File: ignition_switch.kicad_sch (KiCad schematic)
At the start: 8 parts, among them U11 EL3H7, U9 EL3H7

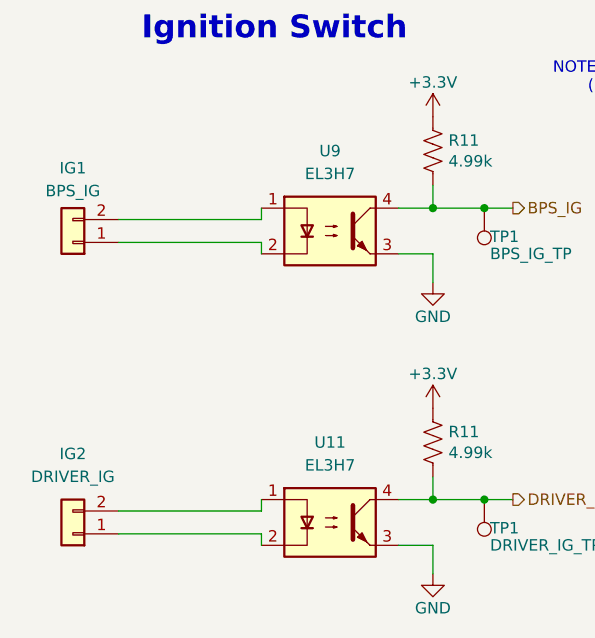
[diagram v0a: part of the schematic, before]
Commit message: Changed optocoupler resistor values, updated Mouser PNs
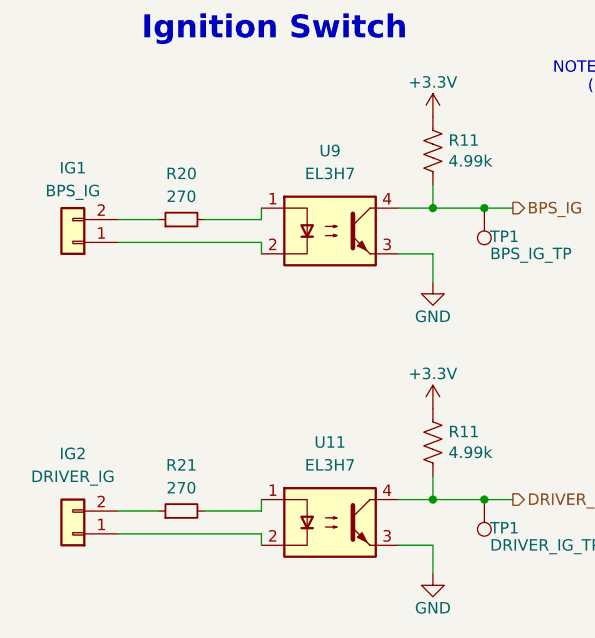
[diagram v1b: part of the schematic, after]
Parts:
- added R20, R21: 270, Resistor_SMD:R_0805_2012Metric, symbol Device:R_Small
- IG1, IG2: Mouser PN (none) -> 538-43650-0215
- R11: Mauser PN 71-CRCW08054K99FKEAC -> (none); Mouser PN (none) -> 71-CRCW08054K99FKEAC
- U11, U9: Mauser PN 638-EL3H7DTAVG -> (none); Mouser PN (none) -> 638-EL3H7DTAVG
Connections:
- net at IG1.2 (Pin_2): now also R20.1; no longer U9.1
- net at U11.1: now also R21.2; no longer IG2.2 (Pin_2)
- new net: IG2.2 (Pin_2), R21.1
- new net: R20.2, U9.1
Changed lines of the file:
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@@
+    (stroke (width 0) (type default))
+  )
+  (wire (pts (xy 122.555 106.68) (xy 128.905 106.68))
     (stroke (width 0) (type default))
   )
@@
     (stroke (width 0) (type default))
   )
-  (wire (pts (xy 113.03 74.295) (xy 128.905 74.295))
+  (wire (pts (xy 122.555 74.295) (xy 128.905 74.295))
+    (stroke (width 0) (type default))
+  )
+  (wire (pts (xy 113.03 74.295) (xy 117.475 74.295))
     (stroke (width 0) (type default))
   )
@@
     (stroke (width 0) (type default))
   )
-  (wire (pts (xy 113.03 106.68) (xy 128.905 106.68))
+  (wire (pts (xy 113.03 106.68) (xy 117.475 106.68))
     (stroke (width 0) (type default))
   )
@@
       (effects (font (size 1.27 1.27)) hide)
     )
+    (property "Mouser PN" "538-43650-0215" (at 107.95 76.835 0)
+      (effects (font (size 1.27 1.27)) hide)
+    )
     (pin "1")
     (pin "2")
@@
       (effects (font (size 1.27 1.27)) (justify left) hide)
     )
-    (property "Mauser PN" "638-EL3H7DTAVG " (at 136.525 107.95 0)
-      (effects (font (size 1.27 1.27)) hide)
-    )
     (property "PN" "EL3H7(D)(TA)-VG" (at 136.525 107.95 0)
+      (effects (font (size 1.27 1.27)) hide)
+    )
+    (property "Mouser PN" "638-EL3H7DTAVG " (at 136.525 107.95 0)
       (effects (font (size 1.27 1.27)) hide)
     )
@@
     )
   )
+  (symbol (lib_id "Device:R_Small") (at 120.015 106.68 90) (unit 1)
+    (in_bom yes) (on_board yes) (dnp no) (fields_autoplaced)
+    (property "Reference" "R21" (at 120.015 101.6 90)
+      (effects (font (size 1.27 1.27)))
+    )
+    (property "Value" "270" (at 120.015 104.14 90)
+      (effects (font (size 1.27 1.27)))
+    )
+    (property "Footprint" "Resistor_SMD:R_0805_2012Metric" (at 120.015 106.68 0)
+      (effects (font (size 1.27 1.27)) hide)
+    )
+    (property "Datasheet" "https://www.vishay.com/docs/20065/rcse3.pdf" (at 120.015 106.68 0)
+      (effects (font (size 1.27 1.27)) hide)
+    )
+    (property "Mouser PN" "71-RCS0805270RFKEA" (at 120.015 106.68 90)
+      (effects (font (size 1.27 1.27)) hide)
+    )
+    (property "PN" "RCS0805270RFKEA" (at 120.015 106.68 90)
+      (effects (font (size 1.27 1.27)) hide)
+    )
+    (pin "1")
+    (pin "2")
+    (instances
+      (project "Controls-LeaderDaughterPCB"
+        (path "/c7871779-04fe-4705-8150-20a4dd0ef44f/0d7b9330-5178-458e-b803-9c8d464fd559"
+          (reference "R21") (unit 1)
+        )
+      )
+    )
+  )
   (symbol (lib_id "Isolator:EL817") (at 136.525 75.565 0) (unit 1)
     (in_bom yes) (on_board yes) (dnp no) (fields_autoplaced)
@@
       (effects (font (size 1.27 1.27)) (justify left) hide)
     )
-    (property "Mauser PN" "638-EL3H7DTAVG " (at 136.525 75.565 0)
-      (effects (font (size 1.27 1.27)) hide)
-    )
     (property "PN" "EL3H7(D)(TA)-VG" (at 136.525 75.565 0)
+      (effects (font (size 1.27 1.27)) hide)
+    )
+    (property "Mouser PN" "638-EL3H7DTAVG " (at 136.525 75.565 0)
       (effects (font (size 1.27 1.27)) hide)
     )
@@
       (effects (font (size 1.27 1.27)) hide)
     )
+    (property "Mouser PN" "538-43650-0215" (at 107.95 109.22 0)
+      (effects (font (size 1.27 1.27)) hide)
+    )
     (pin "1")
     (pin "2")
@@
       (effects (font (size 1.27 1.27)) hide)
     )
-    (property "Mauser PN" "71-CRCW08054K99FKEAC " (at 147.955 66.675 0)
+    (property "Mouser PN" "71-CRCW08054K99FKEAC " (at 147.955 66.675 0)
       (effects (font (size 1.27 1.27)) hide)
     )
@@
       (effects (font (size 1.27 1.27)) hide)
     )
-    (property "Mauser PN" "71-CRCW08054K99FKEAC " (at 147.955 99.06 0)
+    (property "Mouser PN" "71-CRCW08054K99FKEAC " (at 147.955 99.06 0)
       (effects (font (size 1.27 1.27)) hide)
     )
@@
         )
       )
+    )
+  )
+  (symbol (lib_id "Device:R_Small") (at 120.015 74.295 90) (unit 1)
+    (in_bom yes) (on_board yes) (dnp no) (fields_autoplaced)
+    (property "Reference" "R20" (at 120.015 69.215 90)
+      (effects (font (size 1.27 1.27)))
+    )
+    (property "Value" "270" (at 120.015 71.755 90)
+      (effects (font (size 1.27 1.27)))
+    )
+    (property "Footprint" "Resistor_SMD:R_0805_2012Metric" (at 120.015 74.295 0)
+      (effects (font (size 1.27 1.27)) hide)
+    )
+    (property "Datasheet" "https://www.vishay.com/docs/20065/rcse3.pdf" (at 120.015 74.295 0)
+      (effects (font (size 1.27 1.27)) hide)
+    )
+    (property "Mouser PN" "71-RCS0805270RFKEA" (at 120.015 74.295 90)
+      (effects (font (size 1.27 1.27)) hide)
+    )
+    (property "PN" "RCS0805270RFKEA" (at 120.015 74.295 90)
+      (effects (font (size 1.27 1.27)) hide)
+    )
+    (pin "1")
+    (pin "2")
+    (instances
+      (project "Controls-LeaderDaughterPCB"
+        (path "/c7871779-04fe-4705-8150-20a4dd0ef44f/0d7b9330-5178-458e-b803-9c8d464fd559"
+          (reference "R20") (unit 1)
+        )
+      )
